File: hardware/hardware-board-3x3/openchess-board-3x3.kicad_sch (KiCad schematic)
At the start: 46 parts, among them J1 Conn_02x13, U1 DRV5032FC, U2 DRV5032FC, U3 DRV5032FC, U4 DRV5032FC, U5 DRV5032FC, U6 DRV5032FC, U7 DRV5032FC, U8 DRV5032FC, U9 DRV5032FC

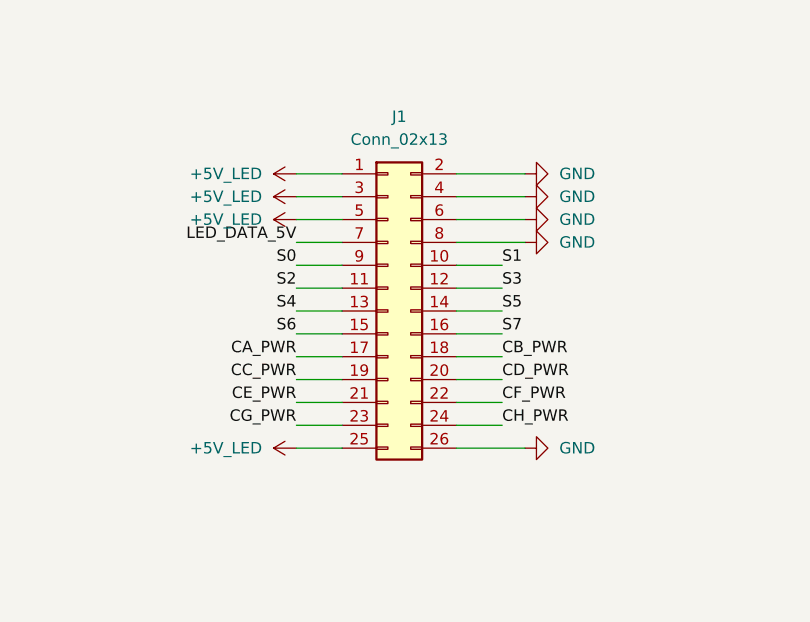
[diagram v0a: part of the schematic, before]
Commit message: Add scripts to merge and tile PDF layers for KiCad projects
- Implemented `merge_pdf_layers.py` to overlay multiple single-page PDFs into one page, allowing for easy printing of layered designs.
- Created `tile_pdf_to_a4.py` to split large PDFs into A4-sized tiles with configurable overlap, facilitating printing on standard home printers.
- Both scripts require the `pypdf` library for PDF manipulation.
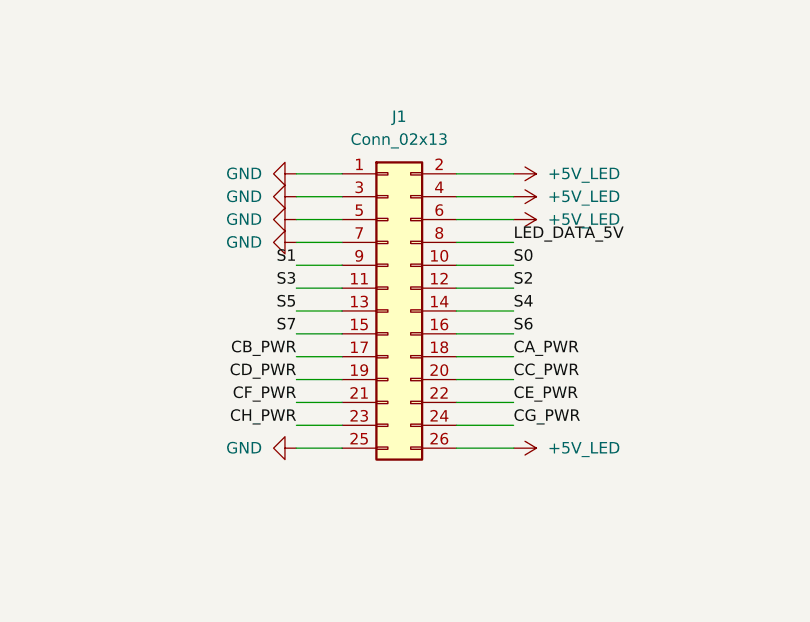
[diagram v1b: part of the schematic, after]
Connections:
- net +5V_LED: now also J1.2 (Pin_2), J1.26 (Pin_26), J1.4 (Pin_4), J1.6 (Pin_6); no longer J1.1 (Pin_1), J1.25 (Pin_25), J1.3 (Pin_3), J1.5 (Pin_5)
- net CA_PWR: now also J1.18 (Pin_18); no longer J1.17 (Pin_17)
- net CB_PWR: now also J1.17 (Pin_17); no longer J1.18 (Pin_18)
- net CC_PWR: now also J1.20 (Pin_20); no longer J1.19 (Pin_19)
- net CD_PWR: now also J1.19 (Pin_19); no longer J1.20 (Pin_20)
- net CE_PWR: now also J1.22 (Pin_22); no longer J1.21 (Pin_21)
- net CF_PWR: now also J1.21 (Pin_21); no longer J1.22 (Pin_22)
- net CG_PWR: now also J1.24 (Pin_24); no longer J1.23 (Pin_23)
- net CH_PWR: now also J1.23 (Pin_23); no longer J1.24 (Pin_24)
- net GND: now also J1.1 (Pin_1), J1.25 (Pin_25), J1.3 (Pin_3), J1.5 (Pin_5), J1.7 (Pin_7); no longer J1.2 (Pin_2), J1.26 (Pin_26), J1.4 (Pin_4), J1.6 (Pin_6), J1.8 (Pin_8)
- net LED_DATA_5V: now also J1.8 (Pin_8); no longer J1.7 (Pin_7)
- net S0: now also J1.10 (Pin_10); no longer J1.9 (Pin_9)
- net S1: now also J1.9 (Pin_9); no longer J1.10 (Pin_10)
- net S2: now also J1.12 (Pin_12); no longer J1.11 (Pin_11)
- net S3: now also J1.11 (Pin_11); no longer J1.12 (Pin_12)
- net S4: now also J1.14 (Pin_14); no longer J1.13 (Pin_13)
- net S5: now also J1.13 (Pin_13); no longer J1.14 (Pin_14)
- net S6: now also J1.16 (Pin_16); no longer J1.15 (Pin_15)
- net S7: now also J1.15 (Pin_15); no longer J1.16 (Pin_16)
